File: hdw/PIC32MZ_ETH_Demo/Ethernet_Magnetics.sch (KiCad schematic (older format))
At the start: 9 parts

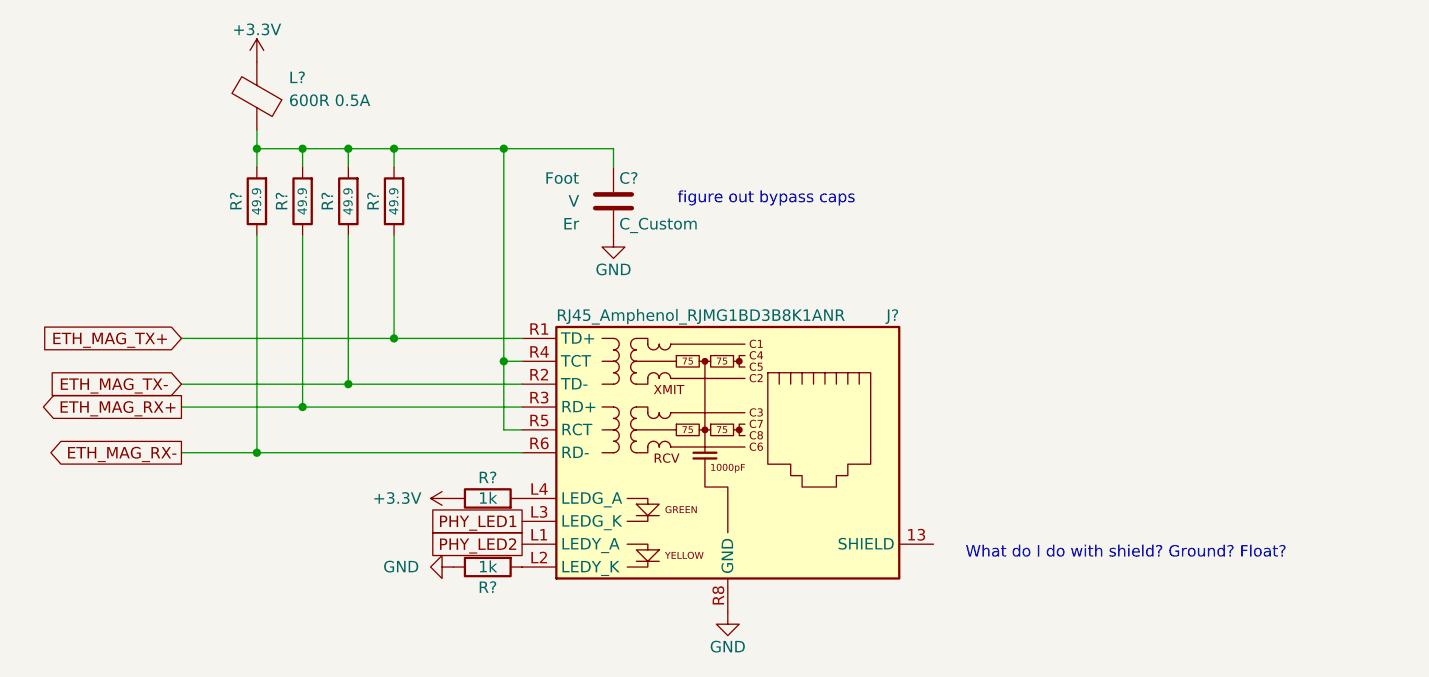
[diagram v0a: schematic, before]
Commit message: More schematic tweaks, followed PHY design guide
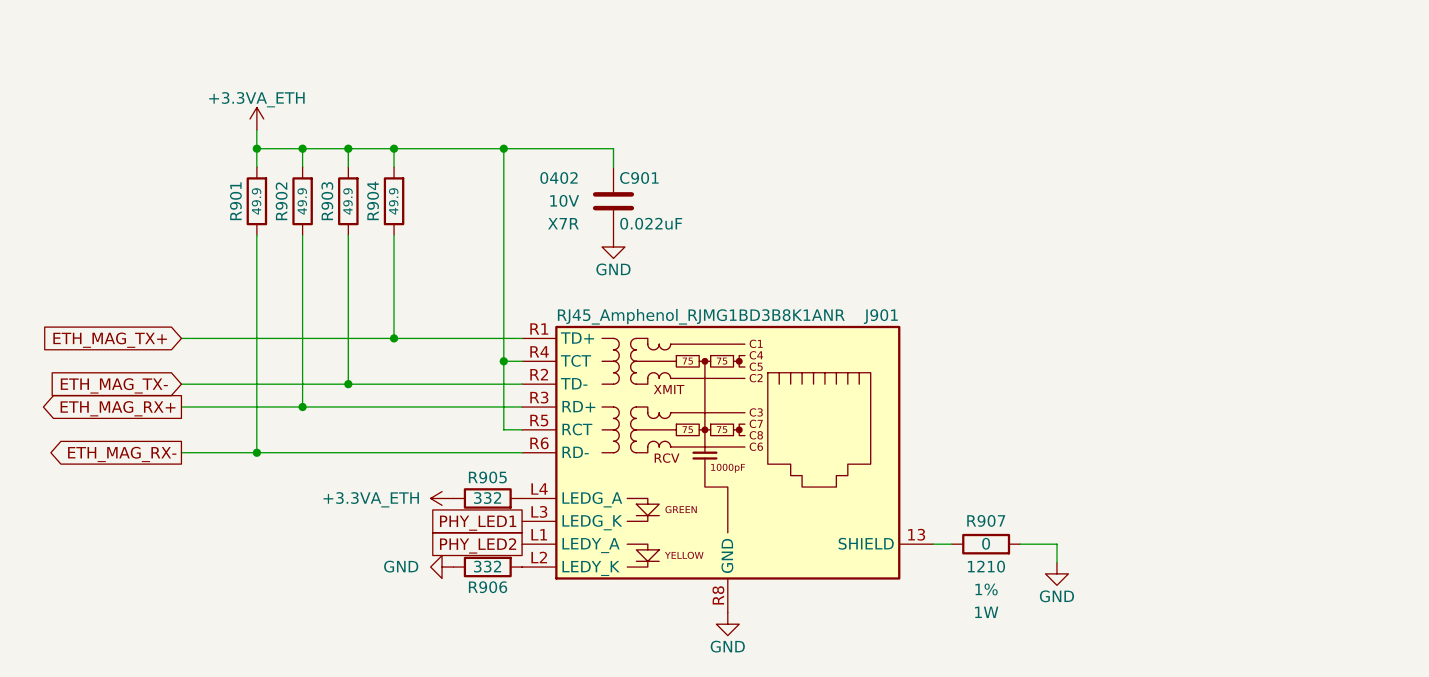
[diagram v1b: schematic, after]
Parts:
- removed L?: 600R 0.5A, Inductors_SMD:L_0603, symbol Device:Ferrite_Bead
- added R907: 0, symbol Custom_Library:R_Custom
- C901: renamed from C?; value C_Custom -> 0.022uF; Dielectric Er -> X7R; Digi-Key PN PN -> (none); Voltage V -> 10V; display_footprint Foot -> 0402
- R905, R906: renamed from R?; value 1k -> 332
- gave numbers to parts that had none: 5
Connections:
- net +3V3 is gone; now on net +3.3VA_ETH: R905.2
- net GND: now also R907.1
- net at J901.13 (SHIELD): now also R907.2
- net +3.3VA_ETH: now reaches C901.1, J901.R4 (TCT), J901.R5 (RCT), R901.1, R902.1, R903.1, R904.1
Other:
- note removed: "What do I do with shield? Ground? Float?"
- note removed: "figure out bypass caps"
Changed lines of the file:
@@
 EESchema Schematic File Version 4
+LIBS:PIC32MZ_ETH_Demo-cache
 EELAYER 30 0
 EELAYER END
@@
 $EndDescr
 $Comp
-L Connector:RJ45_Amphenol_RJMG1BD3B8K1ANR J?
+L Connector:RJ45_Amphenol_RJMG1BD3B8K1ANR J901
 U 1 1 5E6FB5A3
 P 6010 3660
-F 0 "J?" H 6760 4260 50  0000 R CNN
+F 0 "J901" H 6760 4260 50  0000 R CNN
 F 1 "RJ45_Amphenol_RJMG1BD3B8K1ANR" H 5260 4260 50  0000 L CNN
 F 2 "Connector_RJ:RJ45_Amphenol_RJMG1BD3B8K1ANR" H 6010 4360 50  0001 C CNN
@@
 $EndComp
 $Comp
-L power:GND #PWR?
+L power:GND #PWR0905
 U 1 1 5E6FEBC4
 P 6010 4360
-F 0 "#PWR?" H 6010 4110 50  0001 C CNN
+F 0 "#PWR0905" H 6010 4110 50  0001 C CNN
 F 1 "GND" H 6010 4210 50  0000 C CNN
 F 2 "" H 6010 4360 50  0001 C CNN
@@
 AR Path="/5CB6F1ED/5E703AF9" Ref="R?"  Part="1"
 AR Path="/5E6978AF/5E703AF9" Ref="R?"  Part="1"
-AR Path="/5E69796B/5E703AF9" Ref="R?"  Part="1"
-F 0 "R?" V 4460 2560 50  0000 C CNN
+AR Path="/5E69796B/5E703AF9" Ref="R904"  Part="1"
+F 0 "R904" V 4460 2560 50  0000 C CNN
 F 1 "49.9" V 4550 2560 40  0000 C CNN
 F 2 "Resistors_SMD:R_0402" H 4550 2560 50  0001 C CNN
@@
 	1    0    0    -1
 $EndComp
-Text Notes 5790 2580 0    50   ~ 0
-figure out bypass caps
 $Comp
 L Custom_Library:R_Custom R?
@@
 AR Path="/5CB6F1ED/5E7065DF" Ref="R?"  Part="1"
 AR Path="/5E6978AF/5E7065DF" Ref="R?"  Part="1"
-AR Path="/5E69796B/5E7065DF" Ref="R?"  Part="1"
-F 0 "R?" V 4260 2560 50  0000 C CNN
+AR Path="/5E69796B/5E7065DF" Ref="R903"  Part="1"
+F 0 "R903" V 4260 2560 50  0000 C CNN
 F 1 "49.9" V 4350 2560 40  0000 C CNN
 F 2 "Resistors_SMD:R_0402" H 4350 2560 50  0001 C CNN
@@
 AR Path="/5CB6F1ED/5E706980" Ref="R?"  Part="1"
 AR Path="/5E6978AF/5E706980" Ref="R?"  Part="1"
-AR Path="/5E69796B/5E706980" Ref="R?"  Part="1"
-F 0 "R?" V 4060 2560 50  0000 C CNN
+AR Path="/5E69796B/5E706980" Ref="R902"  Part="1"
+F 0 "R902" V 4060 2560 50  0000 C CNN
 F 1 "49.9" V 4150 2560 40  0000 C CNN
 F 2 "Resistors_SMD:R_0402" H 4150 2560 50  0001 C CNN
@@
 AR Path="/5CB6F1ED/5E706D39" Ref="R?"  Part="1"
 AR Path="/5E6978AF/5E706D39" Ref="R?"  Part="1"
-AR Path="/5E69796B/5E706D39" Ref="R?"  Part="1"
-F 0 "R?" V 3860 2560 50  0000 C CNN
+AR Path="/5E69796B/5E706D39" Ref="R901"  Part="1"
+F 0 "R901" V 3860 2560 50  0000 C CNN
 F 1 "49.9" V 3950 2560 40  0000 C CNN
 F 2 "Resistors_SMD:R_0402" H 3950 2560 50  0001 C CNN
@@
 Connection ~ 5030 3260
 $Comp
-L Custom_Library:C_Custom C?
+L Custom_Library:C_Custom C901
 U 1 1 5E70C2FC
 P 5510 2560
-F 0 "C?" H 5535 2660 50  0000 L CNN
-F 1 "C_Custom" H 5535 2460 50  0000 L CNN
+F 0 "C901" H 5535 2660 50  0000 L CNN
+F 1 "0.022uF" H 5535 2460 50  0000 L CNN
 F 2 "" H 5548 2410 50  0001 C CNN
 F 3 "" H 5535 2660 50  0001 C CNN
-F 4 "Foot" H 5360 2660 50  0000 R CNN "display_footprint"
-F 5 "V" H 5360 2560 50  0000 R CNN "Voltage"
-F 6 "Er" H 5360 2460 50  0000 R CNN "Dielectric"
-F 7 "PN" H 5935 3060 60  0001 C CNN "Digi-Key PN"
+F 4 "0402" H 5360 2660 50  0000 R CNN "display_footprint"
+F 5 "10V" H 5360 2560 50  0000 R CNN "Voltage"
+F 6 "X7R" H 5360 2460 50  0000 R CNN "Dielectric"
 	1    5510 2560
 	1    0    0    -1
 $EndComp
 $Comp
-L power:GND #PWR?
+L power:GND #PWR0904
 U 1 1 5E70D82E
 P 5510 2710
-F 0 "#PWR?" H 5510 2460 50  0001 C CNN
+F 0 "#PWR0904" H 5510 2460 50  0001 C CNN
 F 1 "GND" H 5510 2560 50  0000 C CNN
 F 2 "" H 5510 2710 50  0001 C CNN
@@
 	5510 2330 5030 2330
 Connection ~ 5030 2330
-$Comp
-L Device:Ferrite_Bead L?
-U 1 1 5E71175D
-P 3950 2100
-AR Path="/5E6979AC/5E71175D" Ref="L?"  Part="1"
-AR Path="/5E69796B/5E71175D" Ref="L?"  Part="1"
-F 0 "L?" H 3810 2020 50  0000 R CNN
-F 1 "600R 0.5A" H 3810 2120 50  0000 R CNN
-F 2 "Inductors_SMD:L_0603" V 3880 2100 50  0001 C CNN
-F 3 "~" H 3950 2100 50  0001 C CNN
-F 4 "" H -5580 -1660 50  0001 C CNN "Digi-Key PN"
-	1    3950 2100
-	-1   0    0    1
-$EndComp
 Wire Wire Line
 	3950 2250 3950 2330
 Connection ~ 3950 2330
-$Comp
-L power:+3.3V #PWR?
-U 1 1 5E712593
-P 3950 1950
-F 0 "#PWR?" H 3950 1800 50  0001 C CNN
-F 1 "+3.3V" H 3950 2090 50  0000 C CNN
-F 2 "" H 3950 1950 50  0001 C CNN
-F 3 "" H 3950 1950 50  0001 C CNN
-	1    3950 1950
-	1    0    0    -1
-$EndComp
-Text Notes 7050 4130 0    50   ~ 0
-What do I do with shield? Ground? Float?
 Text GLabel 3620 3160 0    50   Input ~ 0
 ETH_MAG_TX+
@@
 AR Path="/5E6ADEF0/5E798CA7" Ref="R?"  Part="1"
 AR Path="/5E69795C/5E798CA7" Ref="R?"  Part="1"
-AR Path="/5E69796B/5E798CA7" Ref="R?"  Part="1"
-F 0 "R?" V 4870 3860 50  0000 C CNN
-F 1 "1k" V 4960 3860 50  0000 C CNN
+AR Path="/5E69796B/5E798CA7" Ref="R905"  Part="1"
+F 0 "R905" V 4870 3860 50  0000 C CNN
+F 1 "332" V 4960 3860 50  0000 C CNN
 F 2 "Resistors_SMD:R_0402" H 4960 3860 50  0001 C CNN
 F 3 "" H 4960 3860 50  0001 C CNN
@@
 AR Path="/5E6ADEF0/5E799642" Ref="R?"  Part="1"
 AR Path="/5E69795C/5E799642" Ref="R?"  Part="1"
-AR Path="/5E69796B/5E799642" Ref="R?"  Part="1"
-F 0 "R?" V 4870 4160 50  0000 C CNN
-F 1 "1k" V 4960 4160 50  0000 C CNN
+AR Path="/5E69796B/5E799642" Ref="R906"  Part="1"
+F 0 "R906" V 4870 4160 50  0000 C CNN
+F 1 "332" V 4960 4160 50  0000 C CNN
 F 2 "Resistors_SMD:R_0402" H 4960 4160 50  0001 C CNN
 F 3 "" H 4960 4160 50  0001 C CNN
@@
 $EndComp
 $Comp
-L power:GND #PWR?
+L power:GND #PWR0903
 U 1 1 5E79A23B
 P 4810 4160
-F 0 "#PWR?" H 4810 3910 50  0001 C CNN
+F 0 "#PWR0903" H 4810 3910 50  0001 C CNN
 F 1 "GND" V 4810 4010 50  0000 R CNN
 F 2 "" H 4810 4160 50  0001 C CNN
@@
 $EndComp
 $Comp
-L power:+3.3V #PWR?
-U 1 1 5E79A7C2
+L Custom_Library:+3.3VA_ETH #PWR0901
+U 1 1 5E842AC4
+P 3950 2250
+F 0 "#PWR0901" H 3950 2100 50  0001 C CNN
+F 1 "+3.3VA_ETH" H 3950 2390 50  0000 C CNN
+F 2 "" H 3950 2250 50  0001 C CNN
+F 3 "" H 3950 2250 50  0001 C CNN
+	1    3950 2250
+	1    0    0    -1
+$EndComp
+Wire Wire Line
+	6990 4060 6910 4060
+$Comp
+L power:GND #PWR0906
+U 1 1 5E8490B5
+P 7450 4140
+F 0 "#PWR0906" H 7450 3890 50  0001 C CNN
+F 1 "GND" H 7450 3990 50  0000 C CNN
+F 2 "" H 7450 4140 50  0001 C CNN
+F 3 "" H 7450 4140 50  0001 C CNN
+	1    7450 4140
+	1    0    0    -1
+$EndComp
+Wire Wire Line
+	7450 4140 7450 4060
+Wire Wire Line
+	7450 4060 7290 4060
+$Comp
+L Custom_Library:+3.3VA_ETH #PWR0902
+U 1 1 5E87711A
 P 4810 3860
-F 0 "#PWR?" H 4810 3710 50  0001 C CNN
-F 1 "+3.3V" V 4810 4000 50  0000 L CNN
+F 0 "#PWR0902" H 4810 3710 50  0001 C CNN
+F 1 "+3.3VA_ETH" V 4810 4220 50  0000 C CNN
 F 2 "" H 4810 3860 50  0001 C CNN
 F 3 "" H 4810 3860 50  0001 C CNN
@@
 	0    -1   -1   0
 $EndComp
+$Comp
+L Custom_Library:R_Custom R907
+U 1 1 5E87981C
+P 7140 4060
+F 0 "R907" V 7040 4060 50  0000 C CNN
+F 1 "0" V 7140 4060 50  0000 C CNN
+F 2 "" H 7140 4060 50  0001 C CNN
+F 3 "" H 7140 4060 50  0001 C CNN
+F 4 "1210" V 7240 4060 50  0000 C CNN "display_footprint"
+F 5 "1%" V 7340 4060 50  0000 C CNN "Tolerance"
+F 6 "1W" V 7440 4060 50  0000 C CNN "Wattage"
+F 7 "PN" H 7440 4460 60  0001 C CNN "Digi-Key PN"
+	1    7140 4060
+	0    1    1    0
+$EndComp
 $EndSCHEMATC

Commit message: Populated digi-key pn's
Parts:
- C901: footprint (none) -> Capacitors_SMD:C_0402; Digi-Key PN (none) -> 311-3793-1-ND
- R901, R902, R903, R904: Digi-Key PN (none) -> 541-3967-1-ND
- R905, R906: Digi-Key PN (none) -> 541-332LCT-ND
- R907: footprint (none) -> Resistors_SMD:R_1210; Digi-Key PN PN -> RMCF1210ZT0R00CT-ND
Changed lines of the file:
@@
 F 5 "1%" H 4630 2560 50  0001 L CNN "Tolerance"
 F 6 "1/16W" H 4630 2480 50  0001 L CNN "Wattage"
+F 7 "541-3967-1-ND" H 4550 2560 50  0001 C CNN "Digi-Key PN"
 	1    4550 2560
 	1    0    0    -1
@@
 F 5 "1%" H 4430 2560 50  0001 L CNN "Tolerance"
 F 6 "1/16W" H 4430 2480 50  0001 L CNN "Wattage"
+F 7 "541-3967-1-ND" H 4350 2560 50  0001 C CNN "Digi-Key PN"
 	1    4350 2560
 	1    0    0    -1
@@
 F 5 "1%" H 4230 2560 50  0001 L CNN "Tolerance"
 F 6 "1/16W" H 4230 2480 50  0001 L CNN "Wattage"
+F 7 "541-3967-1-ND" H 4150 2560 50  0001 C CNN "Digi-Key PN"
 	1    4150 2560
 	1    0    0    -1
@@
 F 5 "1%" H 4030 2560 50  0001 L CNN "Tolerance"
 F 6 "1/16W" H 4030 2480 50  0001 L CNN "Wattage"
+F 7 "541-3967-1-ND" H 3950 2560 50  0001 C CNN "Digi-Key PN"
 	1    3950 2560
 	1    0    0    -1
@@
 F 0 "C901" H 5535 2660 50  0000 L CNN
 F 1 "0.022uF" H 5535 2460 50  0000 L CNN
-F 2 "" H 5548 2410 50  0001 C CNN
+F 2 "Capacitors_SMD:C_0402" H 5548 2410 50  0001 C CNN
 F 3 "" H 5535 2660 50  0001 C CNN
 F 4 "0402" H 5360 2660 50  0000 R CNN "display_footprint"
 F 5 "10V" H 5360 2560 50  0000 R CNN "Voltage"
 F 6 "X7R" H 5360 2460 50  0000 R CNN "Dielectric"
+F 7 "311-3793-1-ND" H 5510 2560 50  0001 C CNN "Digi-Key PN"
 	1    5510 2560
 	1    0    0    -1
@@
 F 5 "1%" H 5030 3860 50  0001 L CNN "Tolerance"
 F 6 "1/16W" H 5030 3790 50  0001 L CNN "Wattage"
+F 7 "541-332LCT-ND" H 4960 3860 50  0001 C CNN "Digi-Key PN"
 	1    4960 3860
 	0    1    1    0
@@
 F 5 "1%" H 5030 4160 50  0001 L CNN "Tolerance"
 F 6 "1/16W" H 5030 4090 50  0001 L CNN "Wattage"
+F 7 "541-332LCT-ND" H 4960 4160 50  0001 C CNN "Digi-Key PN"
 	1    4960 4160
 	0    1    -1   0
@@
 F 0 "R907" V 7040 4060 50  0000 C CNN
 F 1 "0" V 7140 4060 50  0000 C CNN
-F 2 "" H 7140 4060 50  0001 C CNN
+F 2 "Resistors_SMD:R_1210" H 7140 4060 50  0001 C CNN
 F 3 "" H 7140 4060 50  0001 C CNN
 F 4 "1210" V 7240 4060 50  0000 C CNN "display_footprint"
 F 5 "1%" V 7340 4060 50  0000 C CNN "Tolerance"
 F 6 "1W" V 7440 4060 50  0000 C CNN "Wattage"
-F 7 "PN" H 7440 4460 60  0001 C CNN "Digi-Key PN"
+F 7 "RMCF1210ZT0R00CT-ND" H 7440 4460 60  0001 C CNN "Digi-Key PN"
 	1    7140 4060
 	0    1    1    0
